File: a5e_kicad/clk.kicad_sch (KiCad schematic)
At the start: 15 parts, among them U9 AX3HAF1-100.0000, Y2 SIT8924BA-73-18N-25.000000

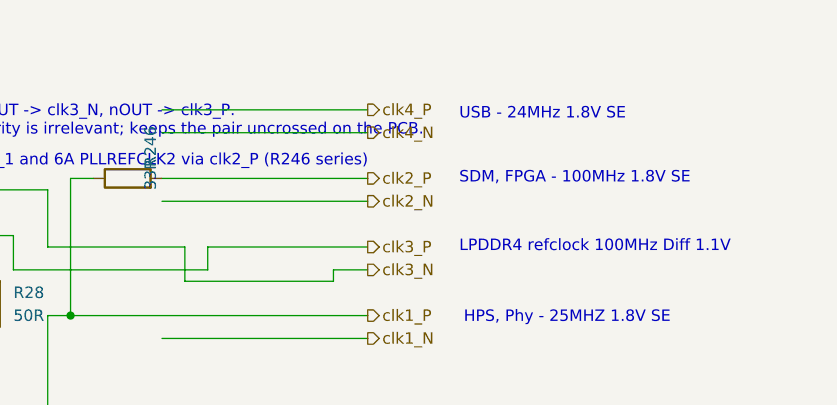
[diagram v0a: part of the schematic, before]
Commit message: Remove unused USB leftovers
USB is not used on this board.
- HPS sheet: remove the {hps_usb} ULPI bus, labels and wires; the 12
  U7 USB0 pins get no-connect flags
- Connectors sheet: remove the {usb_phy} hierarchical label and bus
- Clock sheet: remove the unused clk4 (USB 24 MHz) outputs and note
- Top-level: remove the {hps_usb}, {usb_phy}, clk4_P/clk4_N sheet pins
  and the usb_clk24 net

Netlist compared before/after: only the 12 USB pin nets changed (now
unconnected). ERC 542 -> 522.
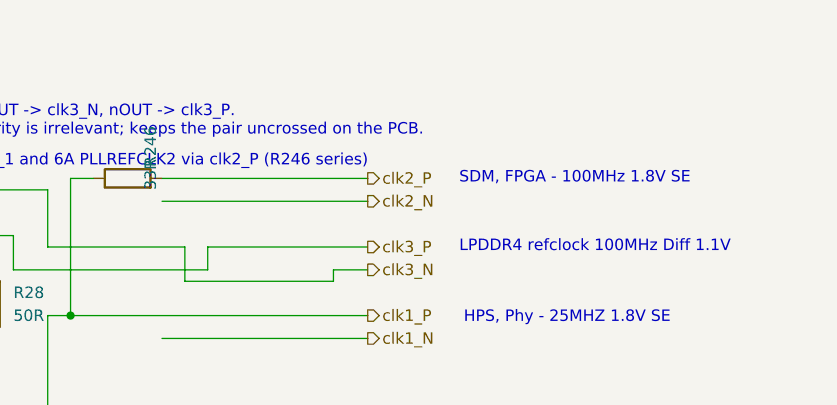
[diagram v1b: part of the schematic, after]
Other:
- note removed: "USB - 24MHz 1.8V SE"
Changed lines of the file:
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@@
-		)
-	)
-	(text "USB - 24MHz 1.8V SE"
-		(exclude_from_sim no)
-		(at 208.28 46.228 0)
-		(effects
-			(font
-				(size 1.27 1.27)
-			)
-			(justify left)
 		)
 	)
@@
 	(wire
 		(pts
-			(xy 175.26 45.72) (xy 198.12 45.72)
-		)
-		(stroke
-			(width 0)
-			(type default)
-		)
-	)
-	(wire
-		(pts
 			(xy 175.26 71.12) (xy 198.12 71.12)
 		)
@@
 		(pts
 			(xy 95.25 43.18) (xy 95.25 48.26)
-		)
-		(stroke
-			(width 0)
-			(type default)
-		)
-	)
-	(wire
-		(pts
-			(xy 175.26 48.26) (xy 198.12 48.26)
 		)
 		(stroke
@@
 		(effects
 			(font
-				(size 1.27 1.27)
-			)
-			(justify left)
-		)
-	)
-	(hierarchical_label "clk4_P"
-		(shape output)
-		(at 198.12 45.72 0)
-		(effects
-			(font
-				(size 1.27 1.27)
-			)
-			(justify left)
-		)
-	)
-	(hierarchical_label "clk4_N"
-		(shape output)
-		(at 198.12 48.26 0)
-		(effects
-			(font

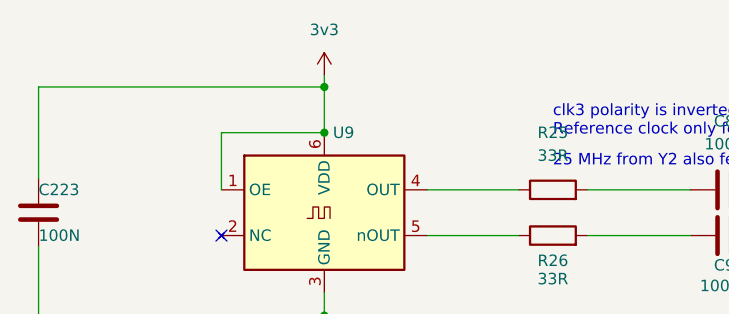
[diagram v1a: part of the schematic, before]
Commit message: Rename lowercase 3v3/1v8 power symbols to 3V3/1V8
KiCad already merged them into the same nets, but every mixed-case pair
raised a similar_power ERC warning. No connectivity change. ERC 503 -> 339.
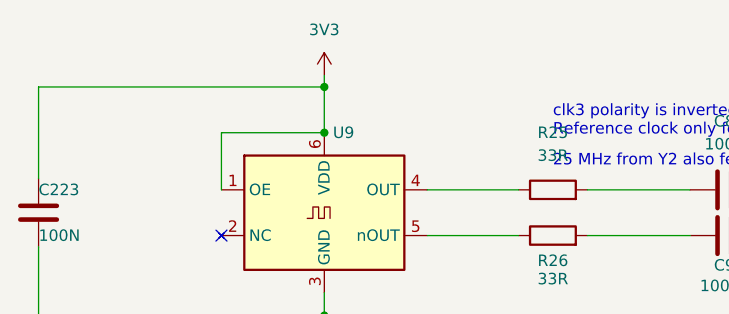
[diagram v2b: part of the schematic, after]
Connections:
- net 3v3 renamed 3V3
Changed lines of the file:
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@@
 			)
 		)
-		(property "Value" "3v3"
+		(property "Value" "3V3"
 			(at 95.25 36.83 0)
 			(show_name no)

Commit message: Add LCSC part numbers and fix C102 footprint
Add a hidden LCSC field to 290 symbols from the JLCPCB parts match
(2026-10-23). Left without LCSC: U7, U15, L1 (not in the JLCPCB
library), C1/C2/C4 and L2-L5 (no value specified), J3 (no confident
match) and Y3 (the 12 pF Basic crystal does not suit the 27 pF load
caps). U2, U12, Y2 and J9 carry the exact-MPN LCSC numbers although
they currently show zero JLCPCB stock.

C102 (22U 6V3) had a 0201 footprint; no 22 uF 0201 part exists. Change
it to 0402 (C415703) like C5-C7.
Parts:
- C222, C223: LCSC (none) -> C190183
- C249: LCSC (none) -> C52923
- C250, C8, C9: LCSC (none) -> C1525
- R244: LCSC (none) -> C11702
- R245: LCSC (none) -> C51721
- R246, R25, R26: LCSC (none) -> C25105
- R27, R28: LCSC (none) -> C25120
- U9: LCSC (none) -> C2003932
- Y2: LCSC (none) -> C17359088
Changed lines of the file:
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@@
+			)
+		)
+		(property "LCSC" "C1525"
+			(at 143.51 58.7248 0)
+			(hide yes)
+			(show_name no)
+			(do_not_autoplace no)
+			(effects
+				(font
+					(size 1.27 1.27)
+				)
 			)
 		)
@@
 			)
 		)
+		(property "LCSC" "C25105"
+			(at 120.65 61.468 90)
+			(hide yes)
+			(show_name no)
+			(do_not_autoplace no)
+			(effects
+				(font
+					(size 1.27 1.27)
+				)
+			)
+		)
 		(property "Datasheet" ""
 			(at 120.65 59.69 0)
@@
 			)
 		)
+		(property "LCSC" "C1525"
+			(at 143.51 53.6448 0)
+			(hide yes)
+			(show_name no)
+			(do_not_autoplace no)
+			(effects
+				(font
+					(size 1.27 1.27)
+				)
+			)
+		)
 		(property "Datasheet" ""
 			(at 139.7 54.61 0)
@@
 			)
 		)
+		(property "LCSC" "C52923"
+			(at 151.13 87.63 0)
+			(hide yes)
+			(show_name no)
+			(do_not_autoplace no)
+			(effects
+				(font
+					(size 1.27 1.27)
+				)
+			)
+		)
 		(property "Datasheet" "~"
 			(at 151.13 87.63 0)
@@
 		)
 		(property "Footprint" "Resistor_SMD:R_0402_1005Metric"
+			(at 135.89 80.01 0)
+			(hide yes)
+			(show_name no)
+			(do_not_autoplace no)
+			(effects
+				(font
+					(size 1.27 1.27)
+				)
+			)
+		)
+		(property "LCSC" "C11702"
 			(at 135.89 80.01 0)
 			(hide yes)
@@
 			)
 		)
+		(property "LCSC" "C25120"
+			(at 149.098 67.31 90)
+			(hide yes)
+			(show_name no)
+			(do_not_autoplace no)
+			(effects
+				(font
+					(size 1.27 1.27)
+				)
+			)
+		)
 		(property "Datasheet" ""
 			(at 147.32 67.31 0)
@@
 			)
 		)
+		(property "LCSC" "C25120"
+			(at 157.988 67.31 90)
+			(hide yes)
+			(show_name no)
+			(do_not_autoplace no)
+			(effects
+				(font
+					(size 1.27 1.27)
+				)
+			)
+		)
 		(property "Datasheet" ""
 			(at 156.21 67.31 0)
@@
 			)
 		)
+		(property "LCSC" "C190183"
+			(at 64.4652 60.96 0)
+			(hide yes)
+			(show_name no)
+			(do_not_autoplace no)
+			(effects
+				(font
+					(size 1.27 1.27)
+				)
+			)
+		)
 		(property "Datasheet" ""
 			(at 63.5 57.15 0)
@@
 			)
 		)
+		(property "LCSC" "C17359088"
+			(at 125.73 118.11 0)
+			(hide yes)
+			(show_name no)
+			(do_not_autoplace no)
+			(effects
+				(font
+					(size 1.27 1.27)
+				)
+			)
+		)
 		(property "Datasheet" "https://www.mouser.com/datasheet/2/371/SiT8924-datasheet-1839508.pdf"
 			(at 105.41 109.22 0)
@@
 		)
 		(property "Footprint" "Resistor_SMD:R_0402_1005Metric"
+			(at 143.51 87.63 0)
+			(hide yes)
+			(show_name no)
+			(do_not_autoplace no)
+			(effects
+				(font
+					(size 1.27 1.27)
+				)
+			)
+		)
+		(property "LCSC" "C51721"
 			(at 143.51 87.63 0)
 			(hide yes)
@@
 			)
 		)
+		(property "LCSC" "C25105"
+			(at 120.65 56.388 90)
+			(hide yes)
+			(show_name no)
+			(do_not_autoplace no)
+			(effects
+				(font
+					(size 1.27 1.27)
+				)
+			)
+		)
 		(property "Datasheet" ""
 			(at 120.65 54.61 0)
@@
 			)
 		)
+		(property "LCSC" "C1525"
+			(at 158.75 87.63 0)
+			(hide yes)
+			(show_name no)
+			(do_not_autoplace no)
+			(effects
+				(font
+					(size 1.27 1.27)
+				)
+			)
+		)
 		(property "Datasheet" "~"
 			(at 158.75 87.63 0)
@@
 			)
 		)
+		(property "LCSC" "C25105"
+			(at 171.45 53.34 90)
+			(hide yes)
+			(show_name no)
+			(do_not_autoplace no)
+			(effects
+				(font
+					(size 1.27 1.27)
+				)
+			)
+		)
 		(property "Datasheet" "~"
 			(at 171.45 53.34 90)
@@
 		)
 		(property "Footprint" "Oscillator:Oscillator_SMD_SiTime_SiT9121-6Pin_3.2x2.5mm"
+			(at 95.25 57.15 0)
+			(hide yes)
+			(show_name no)
+			(do_not_autoplace no)
+			(effects
+				(font
+					(size 1.27 1.27)
+				)
+			)
+		)
+		(property "LCSC" "C2003932"
 			(at 95.25 57.15 0)
 			(hide yes)
@@
 			(at 82.2452 114.3 0)
 			(hide yes)
+			(show_name no)
+			(do_not_autoplace no)
+			(effects
+				(font
+					(size 1.27 1.27)
+				)
+			)
+		)
+		(property "LCSC" "C190183"
+			(at 82.2452 114.3 0)
+			(hide yes)

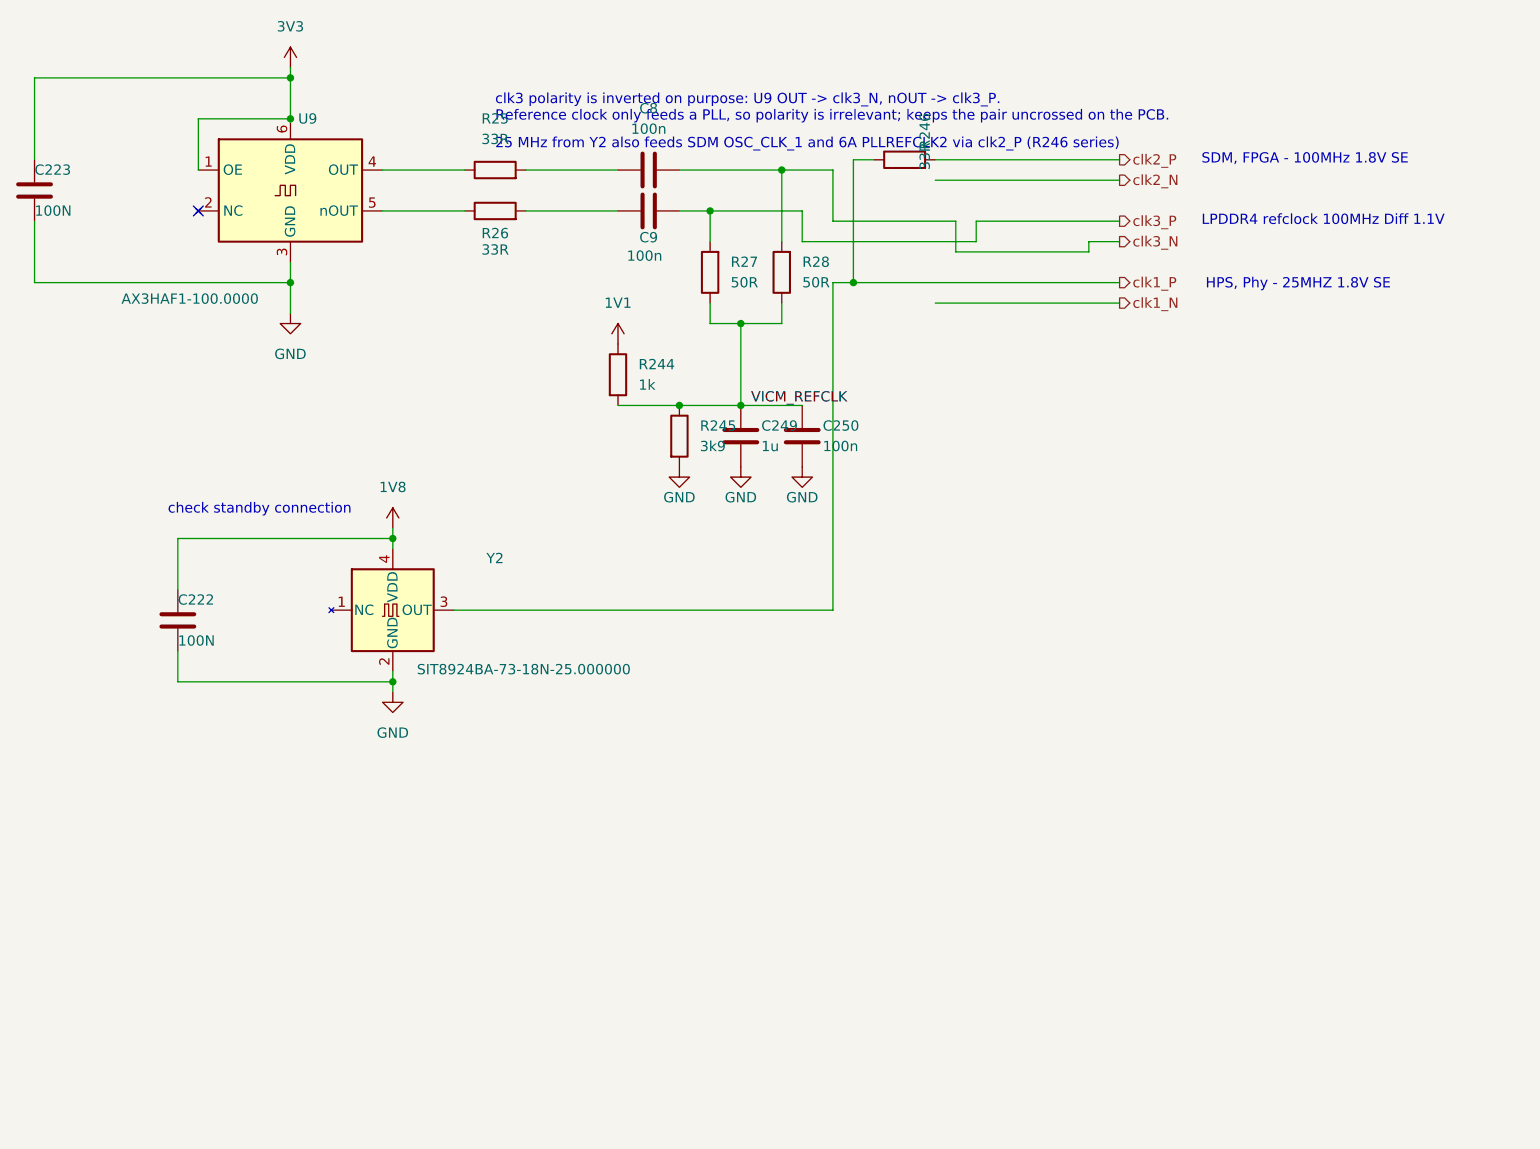
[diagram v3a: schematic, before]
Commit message: Power/config review against the Altera docs: bank 6A, MSEL, resets, fabric clock
Checked against Pin Connection Guidelines 813266, Power Management UG
813161, Configuration UG 813773 and the data sheet 813918; findings are
in AGILEX_POWER_CONFIG_CHECKLIST.md.

- VCCIO_HVIO_6A moves from the VCCPT 1V8 regulator to 3V3. PCG table 32
  requires a dedicated VCCIO_HVIO supply. CE19 no longer takes the 1.8 V
  sdm_clk25.
- Y4 (YXC OT3225100MJBA4SL, 100 MHz 3.3 V CMOS, C4353707) drives the
  dangling clk100 net to AE11 (bank 6G PLLREFCLK1), giving the fabric a
  PLL reference that doesn't depend on the HPS. The clock sheet pin
  clk2_N is renamed clk100.
- MSEL 001 (AS fast) -> 011 (AS normal): fast mode needs all supplies
  ramped within 10 ms, which the sequenced regulators don't guarantee.
  R45 now goes to 1V8, and R4 gets its own GND.
- R264 10k pull-up on HPS_COLD_nRESET (SDM_IO10), as the PCG requires.
- R9/R10 (INIT_DONE/CONF_DONE pull-ups) DNP; the internal pull-downs
  hold the pins low until configuration.
- Note on the fpga_power sheet and the PCB (Cmts.User): ferrite + cap
  isolation filters on the PLL/ADC rails are recommended but not
  fitted yet.
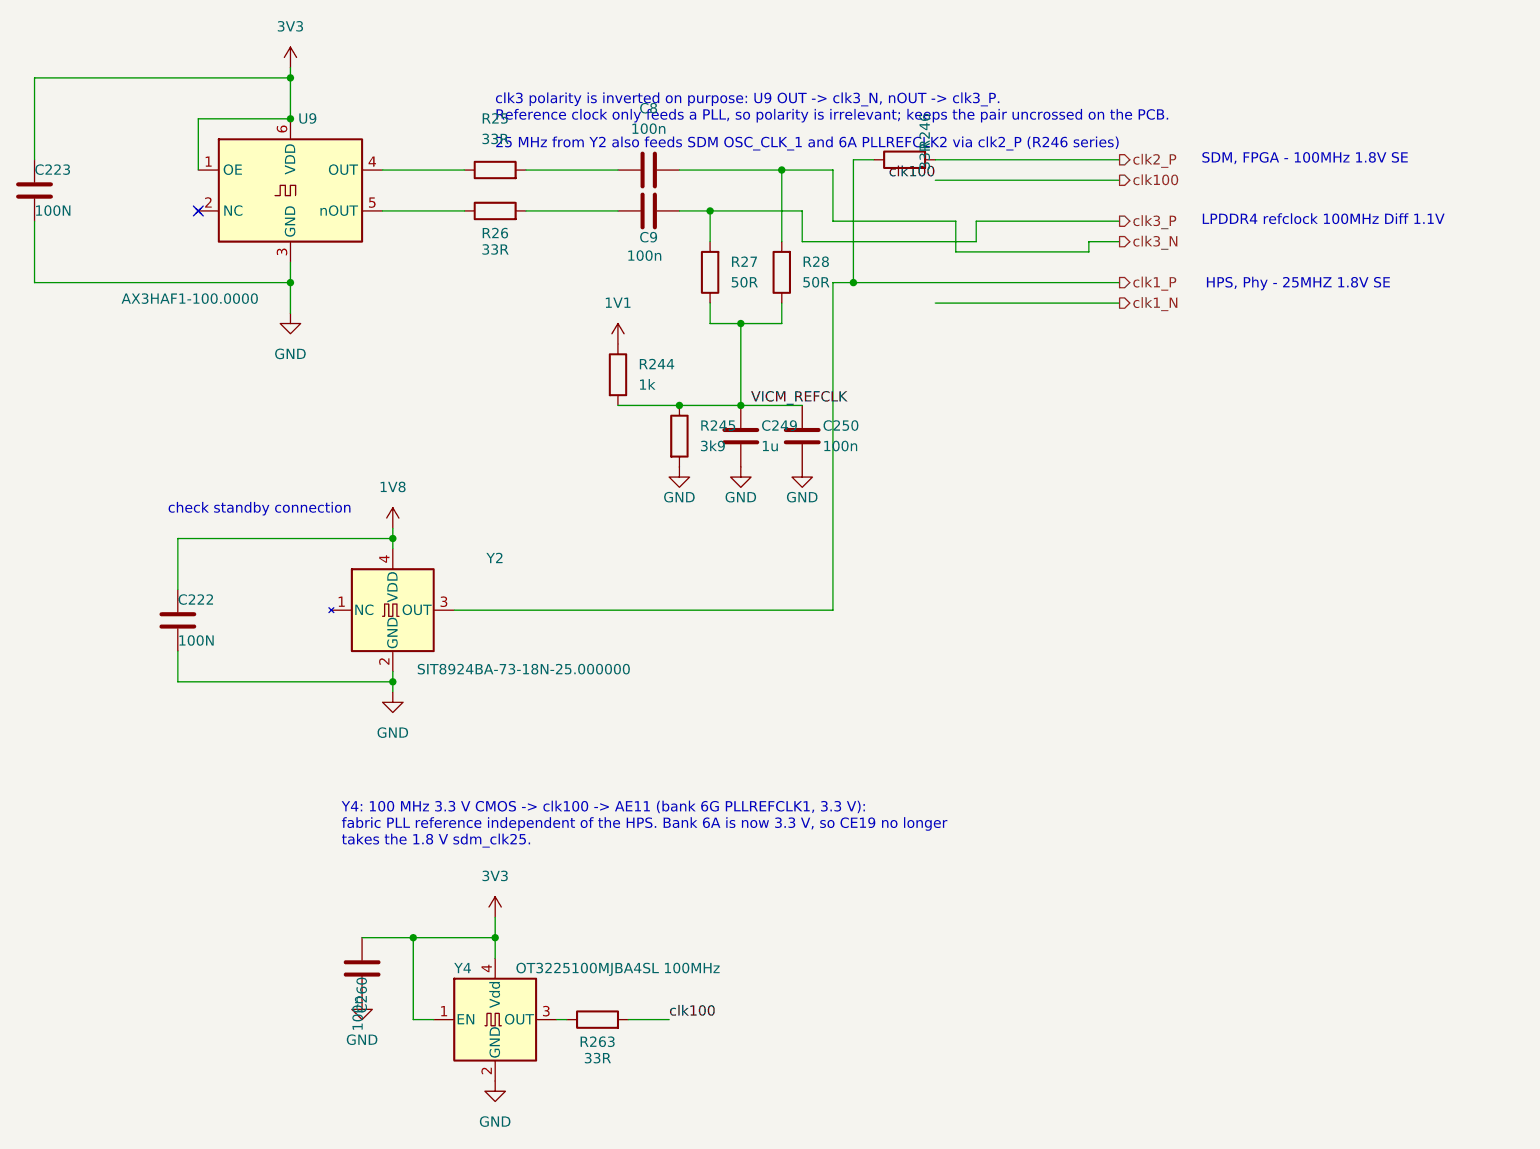
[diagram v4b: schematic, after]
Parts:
- added C260: 100n, Capacitor_SMD:C_0402_1005Metric, symbol Device:C
- added R263: 33R, Resistor_SMD:R_0402_1005Metric, symbol Device:R
- added Y4: OT3225100MJBA4SL 100MHz, Oscillator:Oscillator_SMD_Abracon_ASE-4Pin_3.2x2.5mm, symbol Oscillator:ASE-xxxMHz
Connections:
- net 3V3: now also C260.1, Y4.1 (EN), Y4.4 (Vdd)
- net GND: now also C260.2, Y4.2 (GND)
- new net: R263.1, Y4.3 (OUT)
- new net clk100: R263.2
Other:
- note added: "Y4: 100 MHz 3.3 V CMOS -> clk100 -> AE11 (bank 6G PLLREFCLK1, 3.3 V): fabric PLL reference independent of the HPS. Bank 6A is now 3.3 V, so CE19 no longer takes the 1.8 V sdm_clk25."

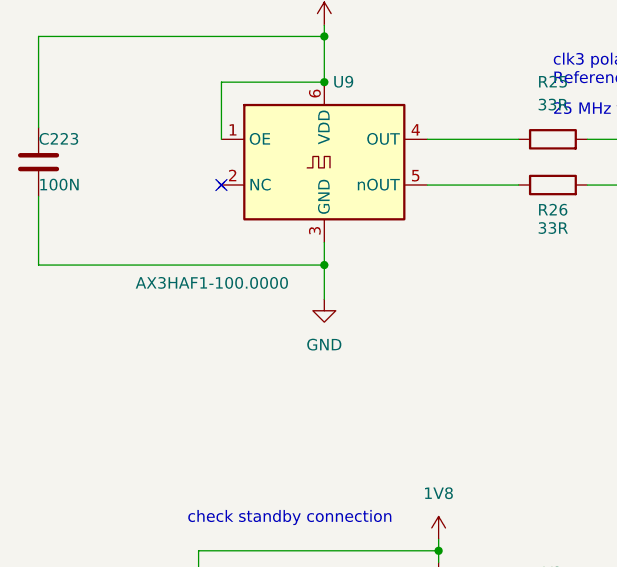
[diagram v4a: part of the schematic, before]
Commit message: U9 to LVDS AX3DAF1, AP61202 dividers to data sheet values
- U9 AX3HAF1 (HCSL) -> AX3DAF1-100.0000T (LVDS, C2002827), same AX3
  pinout. The HCSL part needs 50R to GND at its outputs, which the board
  doesn't have (R27/R28 are behind the AC-coupling caps, to VICM). LVDS
  works with the existing AC coupling, 2x50R termination and bias.
- AP61202 feedback dividers use the data sheet table 1 values with 200k
  top, so the 33 pF feed-forward caps (C116-C119) sit where intended:
  1V8 200k/100k (R81 DNP), 3V3 200k/44.2k, 1V2 200k/200k, 1V1 200k/240k.
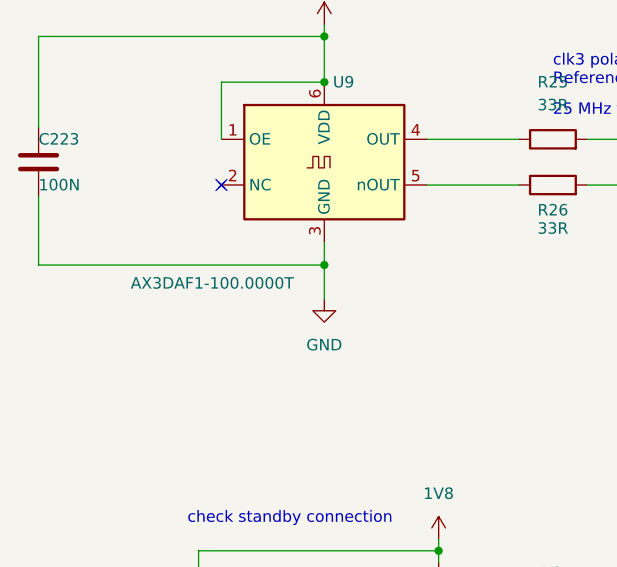
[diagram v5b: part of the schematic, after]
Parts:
- U9: value AX3HAF1-100.0000 -> AX3DAF1-100.0000T; LCSC C2003932 -> C2002827
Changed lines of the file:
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@@
 			)
 		)
-		(property "Value" "AX3HAF1-100.0000"
+		(property "Value" "AX3DAF1-100.0000T"
 			(at 82.804 70.612 0)
 			(show_name no)
@@
 			)
 		)
-		(property "LCSC" "C2003932"
+		(property "LCSC" "C2002827"
 			(at 95.25 57.15 0)
 			(hide yes)
@@
 			)
 		)
-		(property "Description" "100MHz HCSL differential XO, 3.3V, Abracon ClearClock AX3"
+		(property "Description" "Abracon AX3 100 MHz LVDS XO, 3.3 V, 3225-6 (LVDS variant; the HCSL AX3HAF1 needs 50R to GND at its outputs)"
 			(at 95.25 57.15 0)
 			(hide yes)
